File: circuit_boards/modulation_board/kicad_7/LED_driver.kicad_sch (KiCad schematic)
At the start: 11 parts

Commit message: Progress on circuit boards
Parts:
- added C?: 100n, Capacitor_SMD:C_0603_1608Metric, symbol Device:C
- D701, D702, D703, D704, D705: renamed from D?; footprint (none) -> LED_THT:LED_D3.0mm
- R701, R702, R703, R704, R705: renamed from R?; value R -> 390; footprint (none) -> Resistor_SMD:R_0603_1608Metric
- U11: renamed from U?; footprint (none) -> Package_SO:SOIC-16_3.9x9.9mm_P1.27mm
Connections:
- net GND: now also C?.2
- net MODOSC_ON_OFF_LED: now also U11.7 (QH); no longer U11.15 (QA)
- net +3V3 renamed +3.3V
- net +3.3V: now also C?.1
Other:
- moved on the sheet: D701, D702, D703, D704, D705, R701, R702, R703, R704, R705

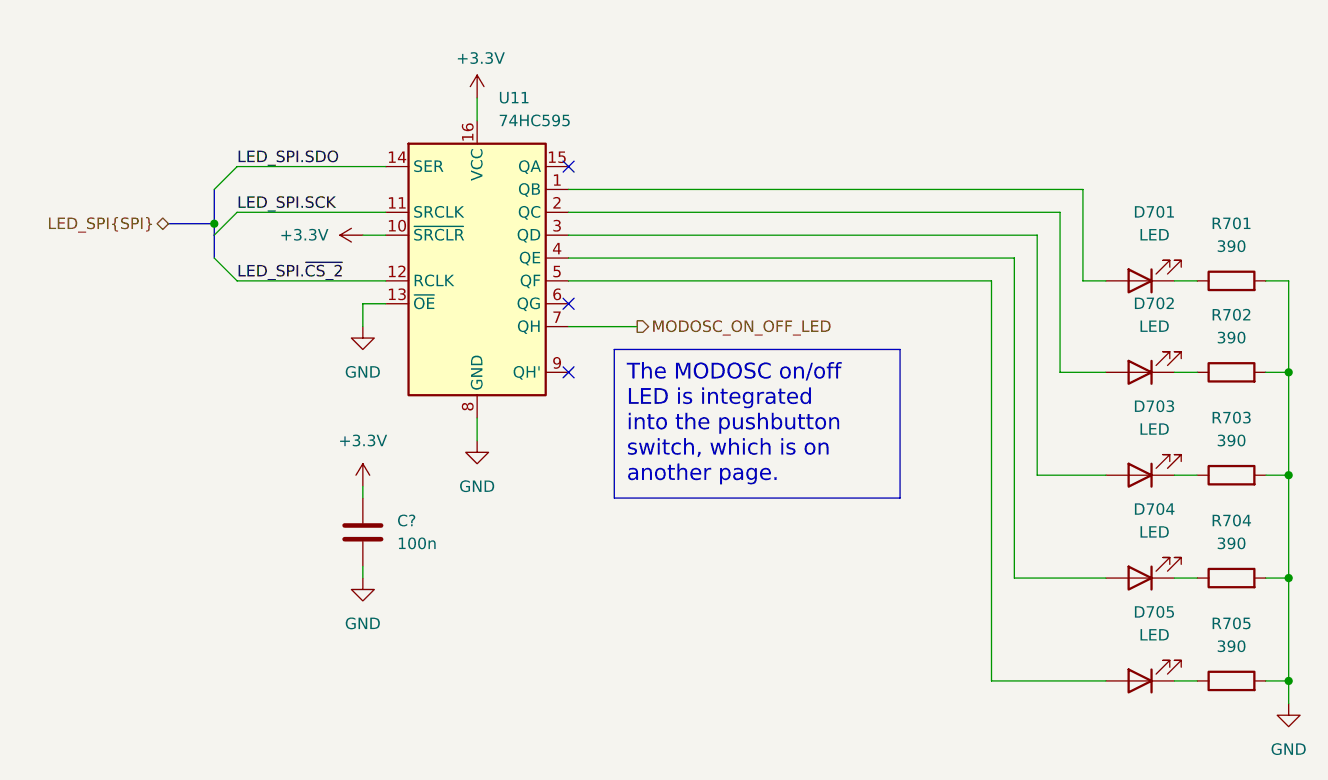
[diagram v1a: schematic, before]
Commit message: Tweaks to mod board, add debug pin
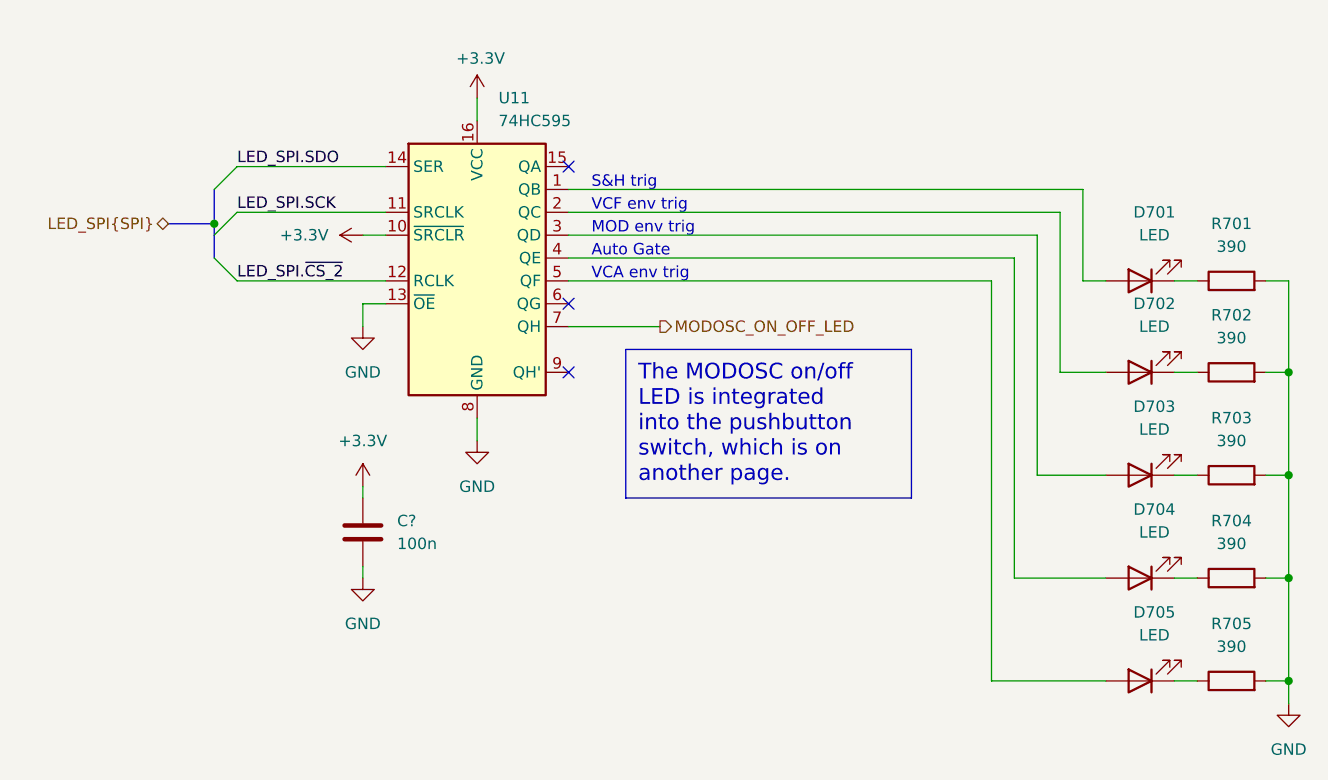
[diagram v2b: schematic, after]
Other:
- note added: "Auto Gate"
- note added: "MOD env trig"
- note added: "S&H trig"
- note added: "VCA env trig"
- note added: "VCF env trig"
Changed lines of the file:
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@@
     (stroke (width 0) (type default))
   )
-  (wire (pts (xy 146.05 99.06) (xy 153.67 99.06))
+  (wire (pts (xy 146.05 99.06) (xy 156.21 99.06))
     (stroke (width 0) (type default))
   )
@@
   )
   (text_box "The MODOSC on/off LED is integrated into the pushbutton switch, which is on another page."
-    (at 151.13 101.6 0) (size 31.75 16.51)
+    (at 152.4 101.6 0) (size 31.75 16.51)
     (stroke (width 0) (type default))
     (fill (type none))
     (effects (font (size 1.75 1.75)) (justify left top))
+  )
+  (text "VCA env trig" (at 148.59 93.98 0)
+    (effects (font (size 1.27 1.27)) (justify left bottom))
+  )
+  (text "VCF env trig" (at 148.59 86.36 0)
+    (effects (font (size 1.27 1.27)) (justify left bottom))
+  )
+  (text "Auto Gate" (at 148.59 91.44 0)
+    (effects (font (size 1.27 1.27)) (justify left bottom))
+  )
+  (text "S&H trig" (at 148.59 83.82 0)
+    (effects (font (size 1.27 1.27)) (justify left bottom))
+  )
+  (text "MOD env trig" (at 148.59 88.9 0)
+    (effects (font (size 1.27 1.27)) (justify left bottom))
   )
   (label "LED_SPI.SCK" (at 109.22 86.36 0) (fields_autoplaced)
@@
     (effects (font (size 1.27 1.27)) (justify right))
   )
-  (hierarchical_label "MODOSC_ON_OFF_LED" (shape output) (at 153.67 99.06 0) (fields_autoplaced)
+  (hierarchical_label "MODOSC_ON_OFF_LED" (shape output) (at 156.21 99.06 0) (fields_autoplaced)
     (effects (font (size 1.27 1.27)) (justify left))
   )

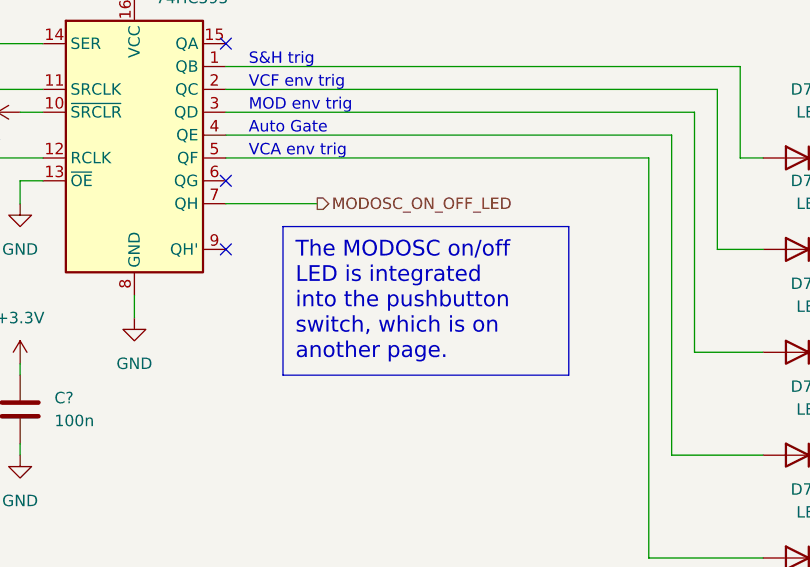
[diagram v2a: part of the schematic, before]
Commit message: Tweaks to mod board, debounce MODOSC toggle switch
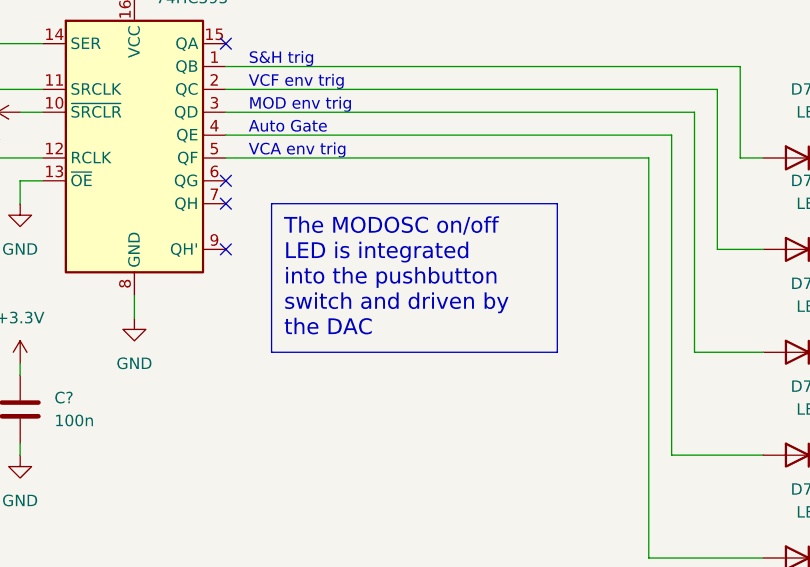
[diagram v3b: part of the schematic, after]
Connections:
- net MODOSC_ON_OFF_LED: no longer names the net of U11.7 (QH)
- no-connect marks 3 -> 4
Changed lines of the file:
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@@
   (title_block
     (title "MICRO-OX Modulation Board")
-    (date "2023-04-13")
+    (date "2023-04-20")
     (rev "0")
     (comment 2 "creativecommons.org/licenses/by/4.0")
@@
   (no_connect (at 146.05 81.28))
   (no_connect (at 146.05 104.14))
+  (no_connect (at 146.05 99.06))
   (no_connect (at 146.05 96.52))
   (bus_entry (at 106.68 88.9) (size 2.54 -2.54)
@@
   )
   (bus (pts (xy 106.68 83.82) (xy 106.68 87.63))
-    (stroke (width 0) (type default))
-  )
-  (wire (pts (xy 146.05 99.06) (xy 156.21 99.06))
     (stroke (width 0) (type default))
   )
@@
     (stroke (width 0) (type default))
   )
-  (text_box "The MODOSC on/off LED is integrated into the pushbutton switch, which is on another page."
-    (at 152.4 101.6 0) (size 31.75 16.51)
+  (text_box "The MODOSC on/off LED is integrated into the pushbutton switch and driven by the DAC"
+    (at 151.13 99.06 0) (size 31.75 16.51)
     (stroke (width 0) (type default))
     (fill (type none))
@@
     (effects (font (size 1.27 1.27)) (justify right))
   )
-  (hierarchical_label "MODOSC_ON_OFF_LED" (shape output) (at 156.21 99.06 0) (fields_autoplaced)
-    (effects (font (size 1.27 1.27)) (justify left))
-  )
   (symbol (lib_id "power:GND") (at 123.19 127 0) (unit 1)

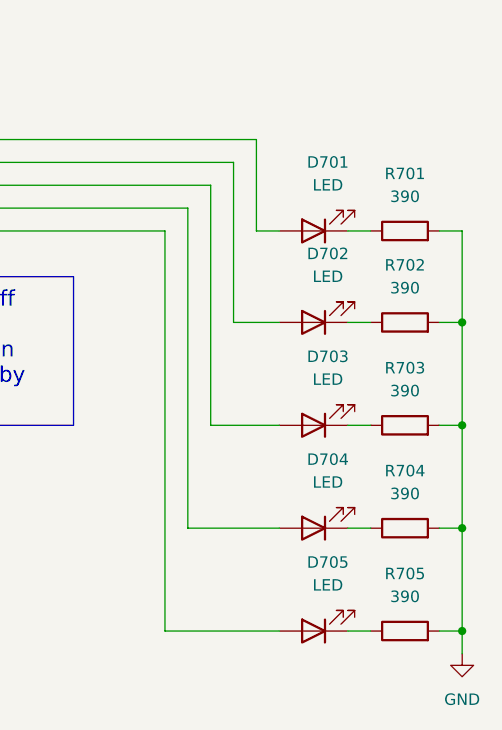
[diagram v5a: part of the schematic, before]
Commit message: Resistor tweaks while evaluating 1st build
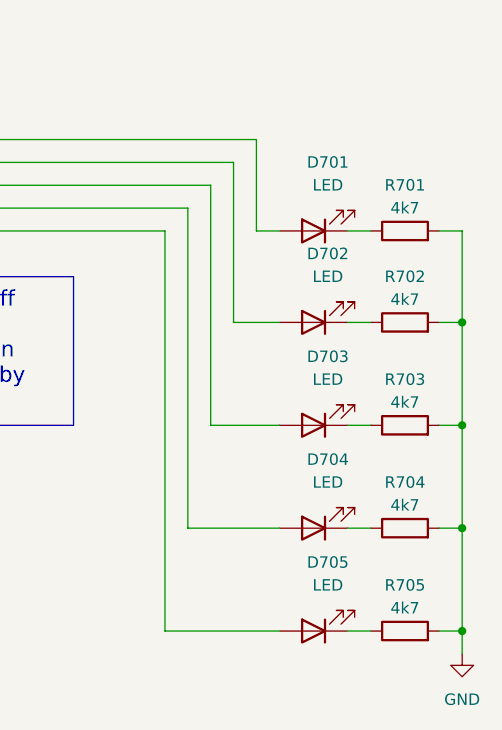
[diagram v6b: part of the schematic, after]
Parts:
- R701, R702, R703, R704, R705: value 390 -> 4k7
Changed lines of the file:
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@@
   (symbol (lib_id "Device:R") (at 219.71 127 90) (unit 1)
     (in_bom yes) (on_board yes) (dnp no) (fields_autoplaced)
-    (property "Reference" "R704" (at 219.71 120.65 90)
-      (effects (font (size 1.27 1.27)))
-    )
-    (property "Value" "390" (at 219.71 123.19 90)
+    (property "Reference" "R704" (at 219.71 121.92 90)
+      (effects (font (size 1.27 1.27)))
+    )
+    (property "Value" "4k7" (at 219.71 124.46 90)
       (effects (font (size 1.27 1.27)))
     )
@@
   (symbol (lib_id "Device:R") (at 219.71 104.14 90) (unit 1)
     (in_bom yes) (on_board yes) (dnp no) (fields_autoplaced)
-    (property "Reference" "R702" (at 219.71 97.79 90)
-      (effects (font (size 1.27 1.27)))
-    )
-    (property "Value" "390" (at 219.71 100.33 90)
+    (property "Reference" "R702" (at 219.71 99.06 90)
+      (effects (font (size 1.27 1.27)))
+    )
+    (property "Value" "4k7" (at 219.71 101.6 90)
       (effects (font (size 1.27 1.27)))
     )
@@
   (symbol (lib_id "Device:R") (at 219.71 93.98 90) (unit 1)
     (in_bom yes) (on_board yes) (dnp no) (fields_autoplaced)
-    (property "Reference" "R701" (at 219.71 87.63 90)
-      (effects (font (size 1.27 1.27)))
-    )
-    (property "Value" "390" (at 219.71 90.17 90)
+    (property "Reference" "R701" (at 219.71 88.9 90)
+      (effects (font (size 1.27 1.27)))
+    )
+    (property "Value" "4k7" (at 219.71 91.44 90)
       (effects (font (size 1.27 1.27)))
     )
@@
   (symbol (lib_id "Device:R") (at 219.71 115.57 90) (unit 1)
     (in_bom yes) (on_board yes) (dnp no) (fields_autoplaced)
-    (property "Reference" "R703" (at 219.71 109.22 90)
-      (effects (font (size 1.27 1.27)))
-    )
-    (property "Value" "390" (at 219.71 111.76 90)
+    (property "Reference" "R703" (at 219.71 110.49 90)
+      (effects (font (size 1.27 1.27)))
+    )
+    (property "Value" "4k7" (at 219.71 113.03 90)
       (effects (font (size 1.27 1.27)))
     )
@@
   (symbol (lib_id "Device:R") (at 219.71 138.43 90) (unit 1)
     (in_bom yes) (on_board yes) (dnp no) (fields_autoplaced)
-    (property "Reference" "R705" (at 219.71 132.08 90)
-      (effects (font (size 1.27 1.27)))
-    )
-    (property "Value" "390" (at 219.71 134.62 90)
-      (effects (font (size 1.27 1.27)))
-    )
+    (property "Reference" "R705" (at 219.71 133.35 90)
+      (effects (font (size 1.27 1.27)))
+    )
+    (property "Value" "4k7" (at 219.71 135.89 90)
+      (effects (font (size 1.27 1.27)))
+    )
